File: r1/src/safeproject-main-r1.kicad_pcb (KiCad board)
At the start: 2 copper layers, 29 x 46.5 mm, 18 parts, among them J1 2842142-4, J2 Conn_01x20

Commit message: Board routed, DRC pass
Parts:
- removed LED1, LED2, LED3: IN-P32TATRGB, LED_SMD:LED_Avago_PLCC4_3.2x2.8mm_CW
- removed R1, R2, R3, R4, R5, R6: 22R, Resistor_SMD:R_0603_1608Metric
- removed R7, R8, R9: 100R, Resistor_SMD:R_0603_1608Metric
- removed the REF** at (0.00, 9.00)
- removed the REF** at (6.00, 0.00)
- removed the REF** at (-6.00, 0.00)
- removed the REF** at (0.00, -9.00)
- added J3: Micro_SD_Card_Det_JAE_ST11, jeffmakes-footprints:microSD_JAE_ST11S008V4H, F.Cu at (-28.2, 8.70)
- added J4: Conn_01x20, Connector_PinHeader_2.54mm:PinHeader_1x20_P2.54mm_Vertical_SMD_Pin1Right, F.Cu at (-3.50, -33.0)
- added J5: Conn_01x20, Connector_PinHeader_2.54mm:PinHeader_1x20_P2.54mm_Vertical, F.Cu at (-10.0, -57.0)
- added REF**: MountingHole_3.2mm_M3_DIN965, MountingHole:MountingHole_3.2mm_M3_DIN965, F.Cu at (21.0, 40.0)
- added REF**: MountingHole_3.2mm_M3_DIN965, MountingHole:MountingHole_3.2mm_M3_DIN965, F.Cu at (-21.0, -40.0)
- added REF**: MountingHole_3.2mm_M3_DIN965, MountingHole:MountingHole_3.2mm_M3_DIN965, F.Cu at (21.0, -40.0)
- J1: value 2842142-4 -> JAE_SIM_Card_SF72S006; footprint jeffmakes-footprints:PinSocket_2x04_P2.00mm_Vertical_SMD_Bottom_or_Top_Entry_AMPMODU -> Connector_JAE:JAE_SIM_Card_SF72S006; moved to F.Cu
- J2: footprint Connector_FFC-FPC:Hirose_FH12-20S-0.5SH_1x20-1MP_P0.50mm_Horizontal -> jeffmakes-footprints:Hirose_FH12-20S-0.5SVA_1x20-1MP_P0.50mm_Vertical; moved to F.Cu
- moved J2 40.4 mm to (8.15, -40.0), turned to 90 degrees
- moved J1 36.4 mm to (-23.2, 21.1), turned to 90 degrees
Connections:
- J2 pad 1: +3V3 -> /+3V3
- J2 pad 2: +3V3 -> /+3V3
- J2 pad 20: +3V3 -> /+3V3
- J2 pad 3: GND -> /GND
- J2 pad 4: GND -> /GND
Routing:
- net /+3V3: track 0.00 -> 106.0 mm
- net +3V3: track 77.0 -> 0.00 mm, vias 5 -> 0
- net /SHDNZ: track 6.49 -> 37.2 mm
- net /SCL: track 10.7 -> 39.4 mm, vias 0 -> 1
- net /FSYNC: track 13.6 -> 37.6 mm, vias 0 -> 1
- net /SDA: track 13.7 -> 33.5 mm
- net /LED2_G: track 34.9 -> 19.0 mm, vias 2 -> 0
- net /SDOUT: track 20.0 -> 34.8 mm, vias 0 -> 1
- net /BCLK: track 16.9 -> 29.6 mm
- net /LED3_R: track 33.9 -> 22.3 mm
- net /LED1_R: track 27.4 -> 19.2 mm, vias 2 -> 0
- net /LED1_G: track 22.3 -> 30.0 mm, vias 2 -> 1
- net Net-(LED1-Pad4): track 7.22 -> 0.00 mm, vias 2 -> 0
- net Net-(LED2-Pad1): track 6.84 -> 0.00 mm
- net Net-(LED3-Pad1): track 6.51 -> 0.00 mm
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- added copper zone on B.Cu, net /GND
- added copper zone on F.Cu, net /GND
- removed copper zone on B.Cu, net GND
- removed copper zone on F.Cu, net GND
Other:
- board size 29 x 46.5 mm -> 57.1 x 122 mm
- board text removed: "1"
- board text removed: "3"
- board text removed: "5"
- board text removed: "7"
- board text removed: "safeacoustics-led-r1 Monad 2021"

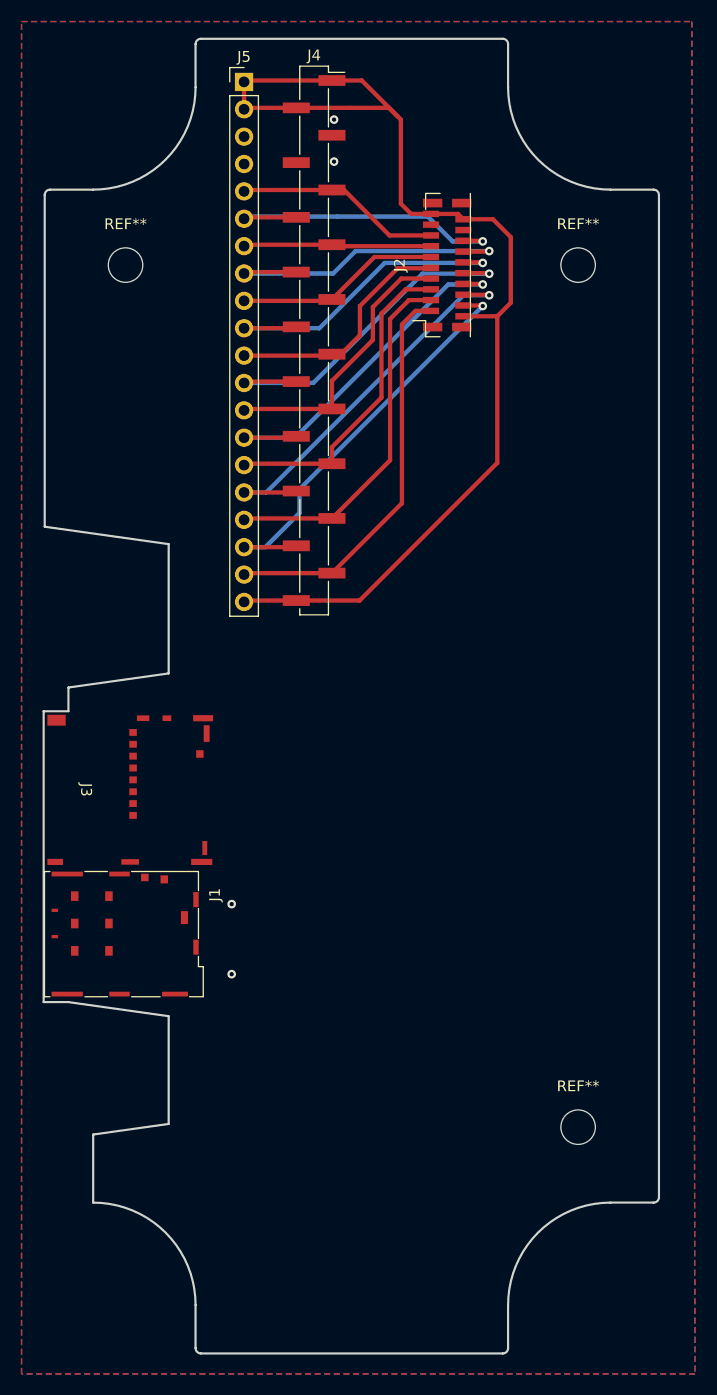
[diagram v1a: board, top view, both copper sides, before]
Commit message: Silkscreen text labelling signals ans pards
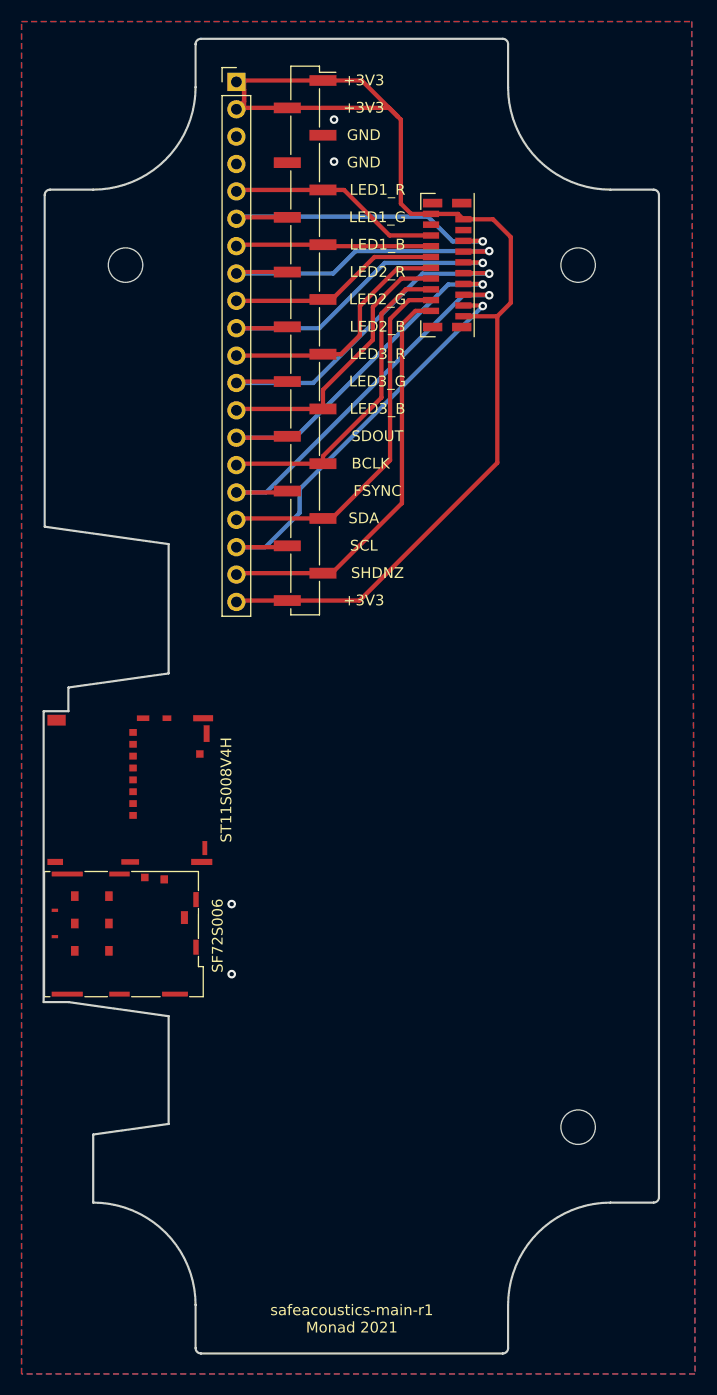
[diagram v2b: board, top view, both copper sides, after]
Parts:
- moved J4 0.83 mm to (-4.33, -33.0)
- moved J5 0.71 mm to (-10.7, -57.0)
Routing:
- net /+3V3: track 106.0 -> 111.3 mm
- net /LED1_G: track 30.0 -> 31.4 mm
- net /SHDNZ: track 37.2 -> 37.9 mm
- net /LED1_R: track 19.2 -> 19.9 mm
- net /LED1_B: track 17.5 -> 18.2 mm
- net /LED3_R: track 22.3 -> 23.0 mm
- net /SDA: track 33.5 -> 34.2 mm
- net /LED2_G: track 19.0 -> 19.7 mm
- net /SDOUT: track 34.8 -> 35.4 mm
- net /SCL: track 39.4 -> 40.0 mm
- net /LED2_B: track 31.4 -> 32.0 mm
- net /FSYNC: track 37.6 -> 38.2 mm
- net /LED2_R: track 30.9 -> 31.5 mm
- net /LED3_G: track 34.3 -> 34.9 mm
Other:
- board text added: "+3V3"
- board text added: "BCLK"
- board text added: "FSYNC"
- board text added: "GND"
- board text added: "LED1_B"
- board text added: "LED1_G"
- board text added: "LED1_R"
- board text added: "LED2_B"
- board text added: "LED2_G"
- board text added: "LED2_R"
- board text added: "LED3_B"
- board text added: "LED3_G"
- board text added: "LED3_R"
- board text added: "SCL"
- board text added: "SDA"
- board text added: "SDOUT"
- board text added: "SF72S006"
- board text added: "SHDNZ"
- board text added: "ST11S008V4H"
- board text added: "safeacoustics-main-r1 Monad 2021"
